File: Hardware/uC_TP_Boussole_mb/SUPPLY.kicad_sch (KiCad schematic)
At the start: 11 parts, among them J1 Conn_01x02, U3 AMS1117-3.3, U5 173010542

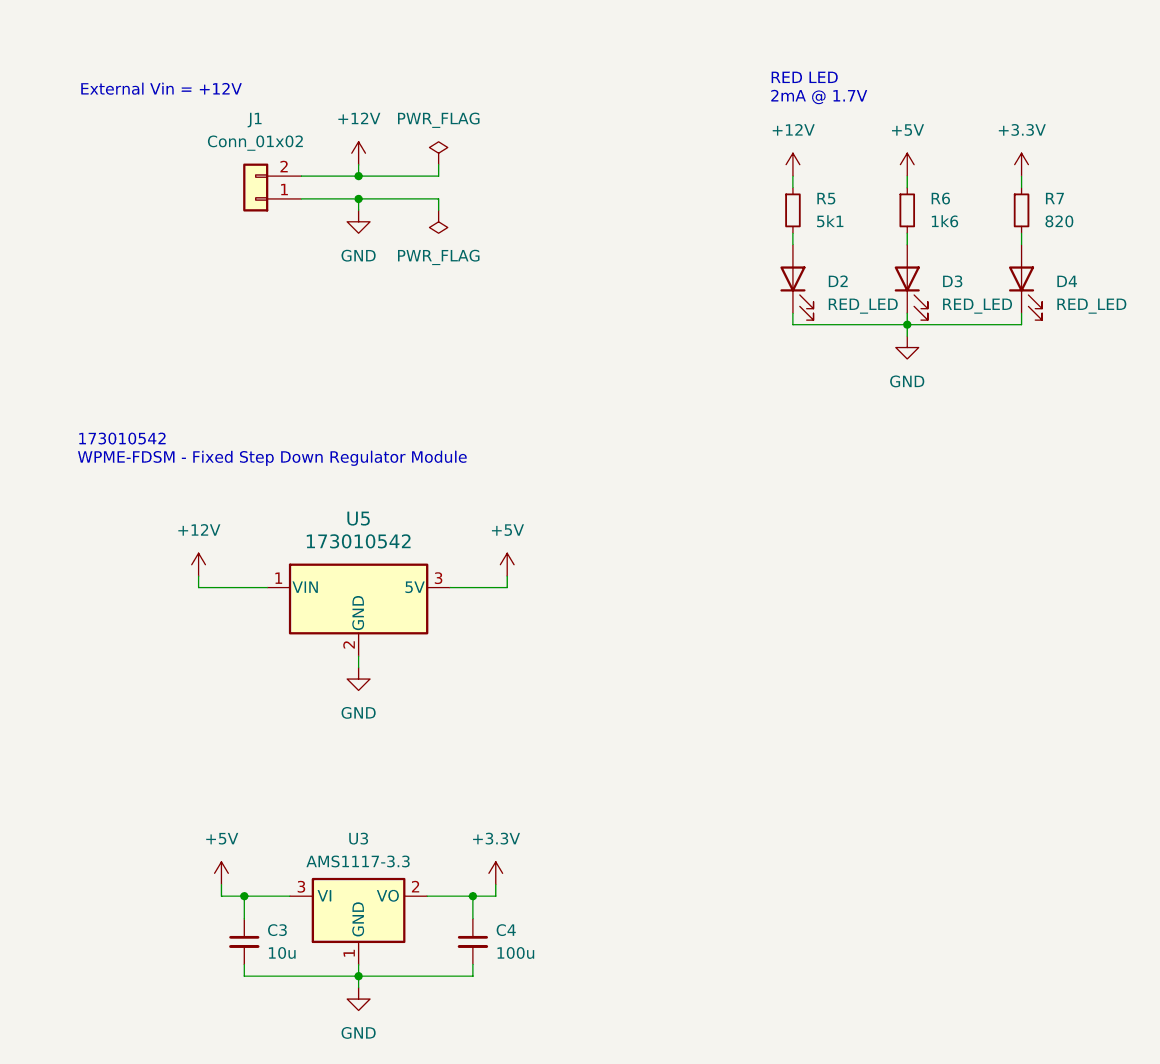
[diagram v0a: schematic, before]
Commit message: starting pin out nucleo
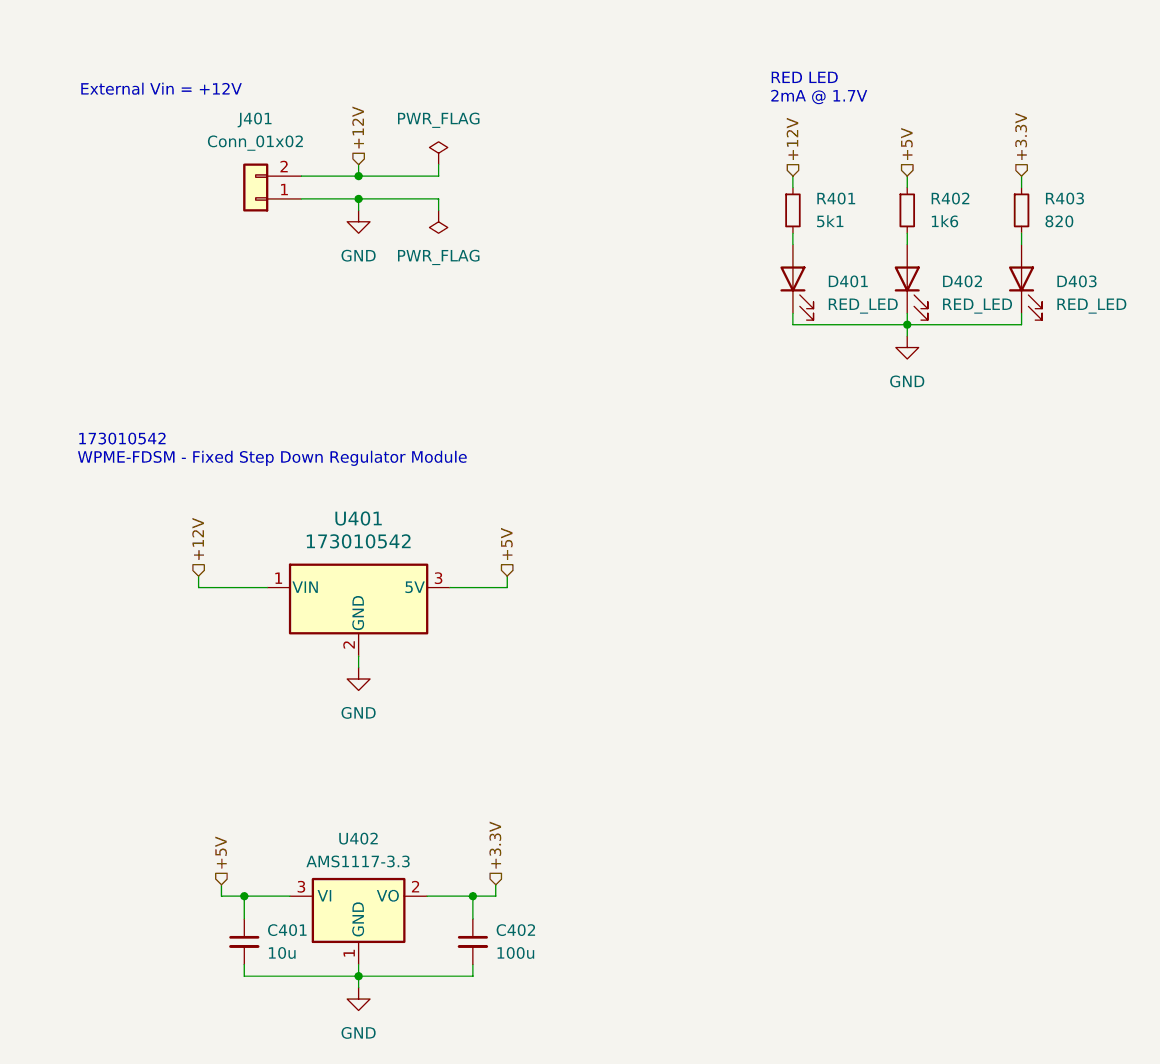
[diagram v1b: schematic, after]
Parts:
- C401: renamed from C3; footprint (none) -> Capacitor_SMD:C_0402_1005Metric
- C402: renamed from C4; footprint (none) -> Capacitor_SMD:C_0402_1005Metric
- D401: renamed from D2; footprint (none) -> LED_SMD:LED_0603_1608Metric
- D402: renamed from D3; footprint (none) -> LED_SMD:LED_0603_1608Metric
- D403: renamed from D4; footprint (none) -> LED_SMD:LED_0603_1608Metric
- J401: renamed from J1; footprint (none) -> Connector_JST:JST_XH_S2B-XH-A_1x02_P2.50mm_Horizontal
- R401: renamed from R5; footprint (none) -> Resistor_SMD:R_0402_1005Metric
- R402: renamed from R6; footprint (none) -> Resistor_SMD:R_0402_1005Metric
- R403: renamed from R7; footprint (none) -> Resistor_SMD:R_0402_1005Metric
- renumbered U5 to U401, U3 to U402

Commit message: update schematic
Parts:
- U401: footprint CONN3_10542_WRE -> (none)
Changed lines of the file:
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@@
 			)
 		)
-		(property "Footprint" "CONN3_10542_WRE"
+		(property "Footprint" ""
 			(at 63.5 88.9 0)
 			(effects

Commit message: ddd
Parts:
- added R404: R_Small, symbol Device:R_Small
- added SW401: SW_SPDT, symbol Switch:SW_SPDT
- U401: footprint (none) -> libs:173010xxx
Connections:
- net +12V: now also SW401.2 (B); no longer J401.2 (Pin_2)
- net GND: now also R404.2
- new net: J401.2 (Pin_2), SW401.1 (A)
- new net: R404.1, SW401.3 (C)
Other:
- moved on the sheet: J401

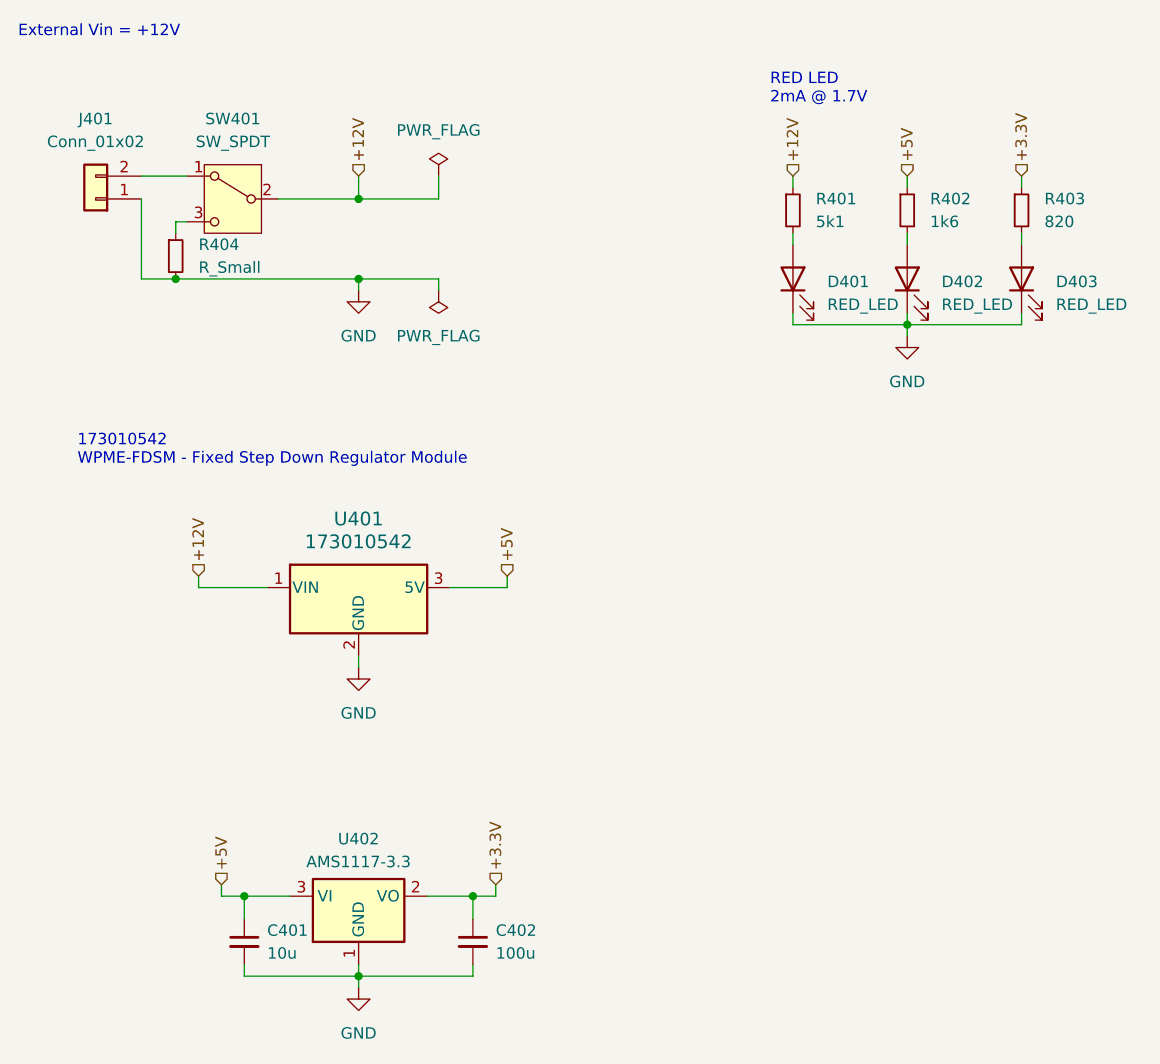
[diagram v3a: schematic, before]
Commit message: update schematic
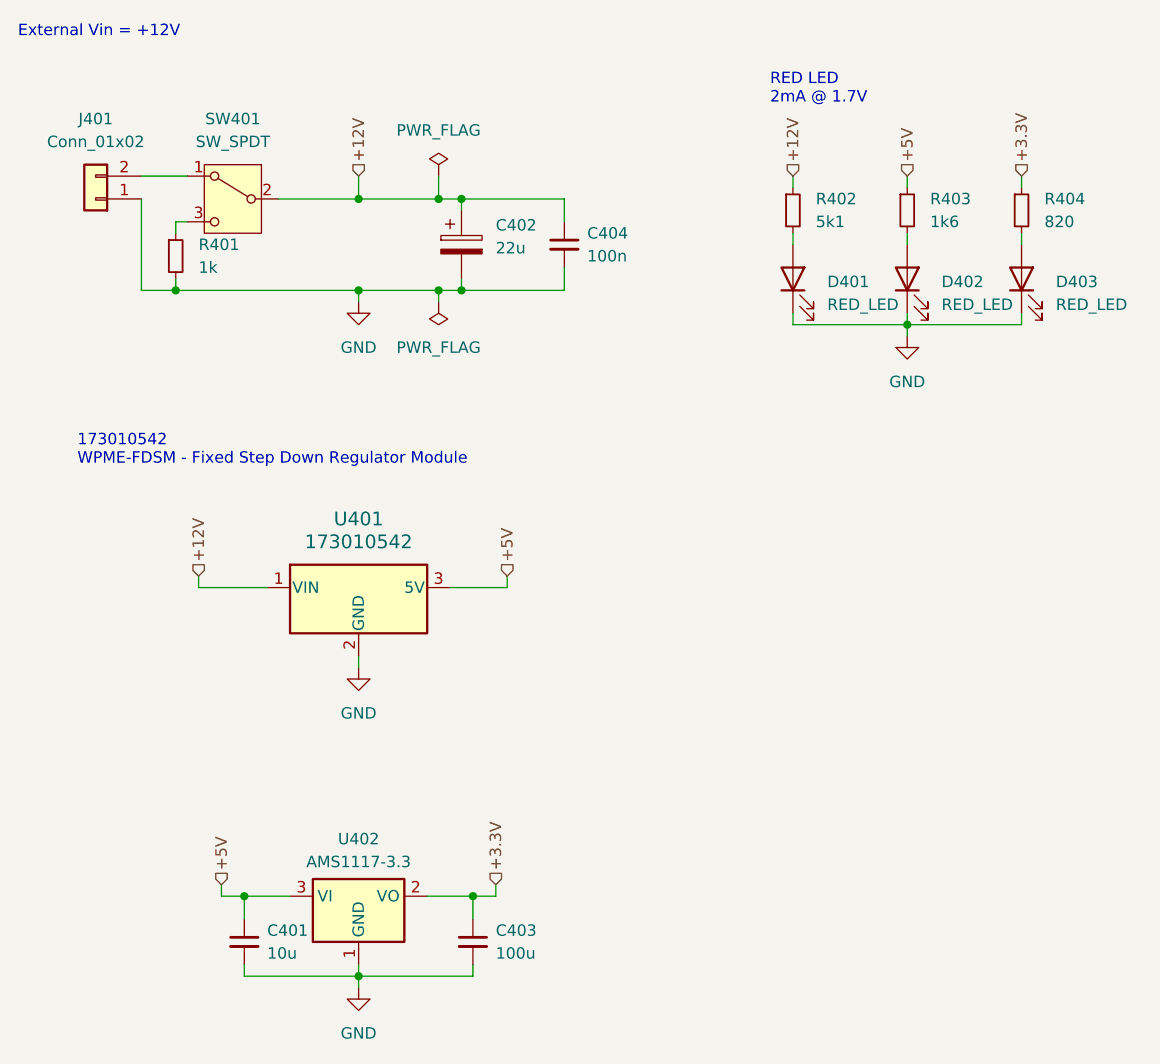
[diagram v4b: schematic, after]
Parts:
- added C402: 22u, Capacitor_SMD:CP_Elec_5x5.4, symbol Device:C_Polarized
- added C404: 100n, Capacitor_SMD:C_0402_1005Metric, symbol Device:C_Small
- R401: renamed from R404; value R_Small -> 1k; footprint (none) -> Resistor_SMD:R_0805_2012Metric
- SW401: footprint (none) -> libs:472121020311; MPN (none) -> 472121020311
- renumbered C402 to C403, R401 to R402, R402 to R403, R403 to R404
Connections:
- net +12V: now also C402.1, C404.1
- net GND: now also C402.2, C404.2

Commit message: finalize pcb
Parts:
- added J402: Conn_02x02_Counter_Clockwise, Connector_PinHeader_2.54mm:PinHeader_2x02_P2.54mm_Vertical_SMD, symbol Connector_Generic:Conn_02x02_Counter_Clockwise
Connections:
- net +12V: now also J402.2 (Pin_2)
- net +3.3V: now also J402.3 (Pin_3)
- net +5V: now also J402.4 (Pin_4)
- net GND: now also J402.1 (Pin_1)
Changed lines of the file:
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@@
+		)
+	)
+	(hierarchical_label "+3.3V"
+		(shape input)
+		(at 123.19 78.74 0)
+		(fields_autoplaced yes)
+		(effects
+			(font
+				(size 1.27 1.27)
+			)
+			(justify left)
 		)
 	)
@@
 	(hierarchical_label "+12V"
 		(shape input)
-		(at 50.8 30.48 90)
+		(at 110.49 78.74 180)
 		(fields_autoplaced yes)
 		(effects
@@
 				(size 1.27 1.27)
 			)
+			(justify right)
+		)
+	)
+	(hierarchical_label "+12V"
+		(shape input)
+		(at 50.8 30.48 90)
+		(fields_autoplaced yes)
+		(effects
+			(font
+				(size 1.27 1.27)
+			)
 			(justify left)
 		)
@@
 	(hierarchical_label "+5V"
 		(shape input)
-		(at 111.76 30.48 90)
+		(at 123.19 76.2 0)
 		(fields_autoplaced yes)
 		(effects
@@
 		)
 	)
+	(hierarchical_label "+5V"
+		(shape input)
+		(at 111.76 30.48 90)
+		(fields_autoplaced yes)
+		(effects
+			(font
+				(size 1.27 1.27)
+			)
+			(justify left)
+		)
+	)
 	(hierarchical_label "+3.3V"
 		(shape input)
@@
 	)
 	(symbol
+		(lib_id "power:GND")
+		(at 110.49 76.2 270)
+		(unit 1)
+		(exclude_from_sim no)
+		(in_bom yes)
+		(on_board yes)
+		(dnp no)
+		(fields_autoplaced yes)
+		(property "Reference" "#PWR0405"
+			(at 104.14 76.2 0)
+			(effects
+				(font
+					(size 1.27 1.27)
+				)
+				(hide yes)
+			)
+		)
+		(property "Value" "GND"
+			(at 106.68 76.1999 90)
+			(effects
+				(font
+					(size 1.27 1.27)
+				)
+				(justify right)
+			)
+		)
+		(property "Footprint" ""
+			(at 110.49 76.2 0)
+			(effects
+				(font
+					(size 1.27 1.27)
+				)
+				(hide yes)
+			)
+		)
+		(property "Datasheet" ""
+			(at 110.49 76.2 0)
+			(effects
+				(font
+					(size 1.27 1.27)
+				)
+				(hide yes)
+			)
+		)
+		(property "Description" "Power symbol creates a global label with name \"GND\" , ground"
+			(at 110.49 76.2 0)
+			(effects
+				(font
+					(size 1.27 1.27)
+				)
+				(hide yes)
+			)
+		)
+		(pin "1"
+		)
+		(instances
+			(project "uC_TP_Boussole_mb"
+				(path "/2e9feef3-d2ce-488a-99fa-e1de5099ffc3/656cbb3c-4322-42f9-a353-72af4bbcd3ec"
+					(reference "#PWR0405")
+					(unit 1)
+				)
+			)
+		)
+	)
+	(symbol
 		(lib_id "Device:R_Small")
 		(at 30.48 39.37 0)
@@
 					(unit 1)
 				)
+			)
+		)
+	)
+	(symbol
+		(lib_id "Connector_Generic:Conn_02x02_Counter_Clockwise")
+		(at 115.57 76.2 0)
+		(unit 1)
+		(exclude_from_sim no)
+		(in_bom yes)
+		(on_board yes)
+		(dnp no)
+		(fields_autoplaced yes)
+		(property "Reference" "J402"
+			(at 116.84 69.85 0)
+			(effects
+				(font
+					(size 1.27 1.27)
+				)
+			)
+		)
+		(property "Value" "Conn_02x02_Counter_Clockwise"
+			(at 116.84 72.39 0)
+			(effects
+				(font
+					(size 1.27 1.27)
+				)
+			)
+		)
+		(property "Footprint" "Connector_PinHeader_2.54mm:PinHeader_2x02_P2.54mm_Vertical_SMD"
+			(at 115.57 76.2 0)
+			(effects
+				(font
+					(size 1.27 1.27)
+				)
+				(hide yes)
+			)
+		)
+		(property "Datasheet" "https://www.we-online.com/components/products/datasheet/61000421121.pdf"
+			(at 115.57 76.2 0)
+			(effects
+				(font
+					(size 1.27 1.27)
+				)
+				(hide yes)
+			)
+		)
+		(property "Description" "Generic connector, double row, 02x02, counter clockwise pin numbering scheme (similar to DIP package numbering), script generated (kicad-library-utils/schlib/autogen/connector/)"
+			(at 115.57 76.2 0)
+			(effects
+				(font
+					(size 1.27 1.27)
+				)
+				(hide yes)
+			)
+		)
+		(property "MPN" "61000421121"
+			(at 115.57 76.2 0)
+			(effects
+				(font
+					(size 1.27 1.27)
+				)
+				(hide yes)
+			)
+		)
+		(pin "2"
+		)
+		(pin "1"
+		)
+		(pin "4"
+		)
+		(pin "3"
+		)
+		(instances
+			(project "uC_TP_Boussole_mb"
+				(path "/2e9feef3-d2ce-488a-99fa-e1de5099ffc3/656cbb3c-4322-42f9-a353-72af4bbcd3ec"
+					(reference "J402")
+					(unit 1)
+				)

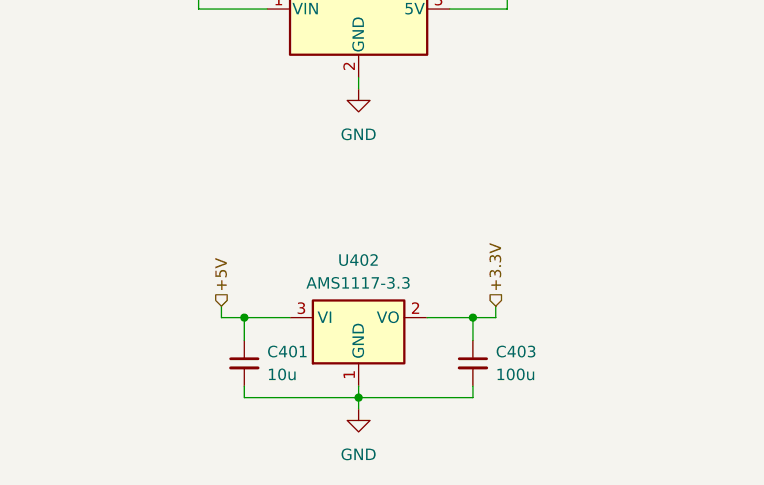
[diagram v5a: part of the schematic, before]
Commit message: create BOM, update MPN
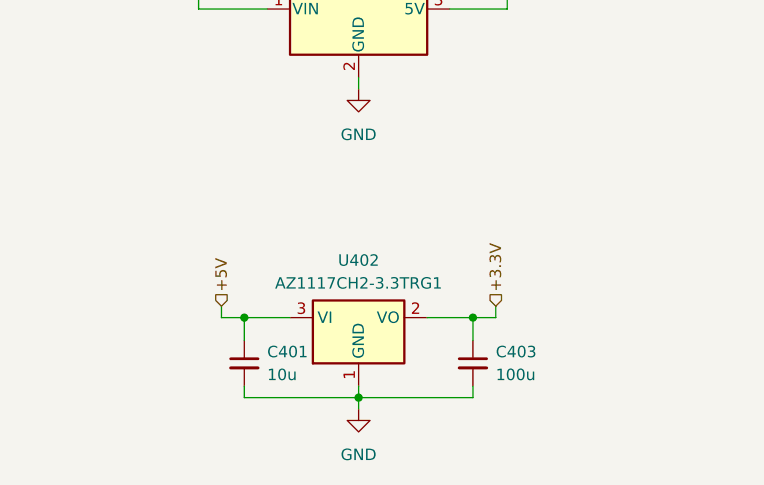
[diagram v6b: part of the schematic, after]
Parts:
- U402: value AMS1117-3.3 -> AZ1117CH2-3.3TRG1; MPN (none) -> AZ1117CH2-3.3TRG1
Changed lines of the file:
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@@
 			)
 		)
-		(property "Value" "AMS1117-3.3"
+		(property "Value" "AZ1117CH2-3.3TRG1"
 			(at 50.8 106.68 0)
 			(effects
@@
 			)
 		)
-		(property "Datasheet" "http://www.advanced-monolithic.com/pdf/ds1117.pdf"
+		(property "Datasheet" "https://4donline.ihs.com/images/VipMasterIC/IC/DIOD/DIOD-S-A0007713706/DIOD-S-A0007713706-1.pdf?hkey=6D3A4C79FDBF58556ACFDE234799DDF0"
 			(at 53.34 116.84 0)
 			(effects
@@
 			(at 50.8 110.49 0)
 			(effects
+				(font
+					(size 1.27 1.27)
+				)
+				(hide yes)
+			)
+		)
+		(property "MPN" "AZ1117CH2-3.3TRG1"
+			(at 50.8 110.49 0)
+			(effects

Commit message: bom
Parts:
- D401, D402, D403: MPN 150060RS55040 -> WE 150060RS55040
- J402: MPN 61000421121 -> WE 61000421121
- SW401: MPN 472121020311 -> WE 472121020311
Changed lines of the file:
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@@
 			)
 		)
-		(property "MPN" "150060RS55040"
+		(property "MPN" "WE 150060RS55040"
 			(at 111.76 41.91 90)
 			(effects
@@
 			)
 		)
-		(property "MPN" "150060RS55040"
+		(property "MPN" "WE 150060RS55040"
 			(at 124.46 41.91 90)
 			(effects
@@
 			)
 		)
-		(property "MPN" "472121020311"
+		(property "MPN" "WE 472121020311"
 			(at 36.83 33.02 0)
 			(effects
@@
 			)
 		)
-		(property "MPN" "61000421121"
+		(property "MPN" "WE 61000421121"
 			(at 115.57 76.2 0)
 			(effects
@@
 			)
 		)
-		(property "MPN" "150060RS55040"
+		(property "MPN" "WE 150060RS55040"
 			(at 99.06 41.91 90)
 			(effects
